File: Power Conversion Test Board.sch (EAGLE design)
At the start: 18 parts, among them U1 LM2678

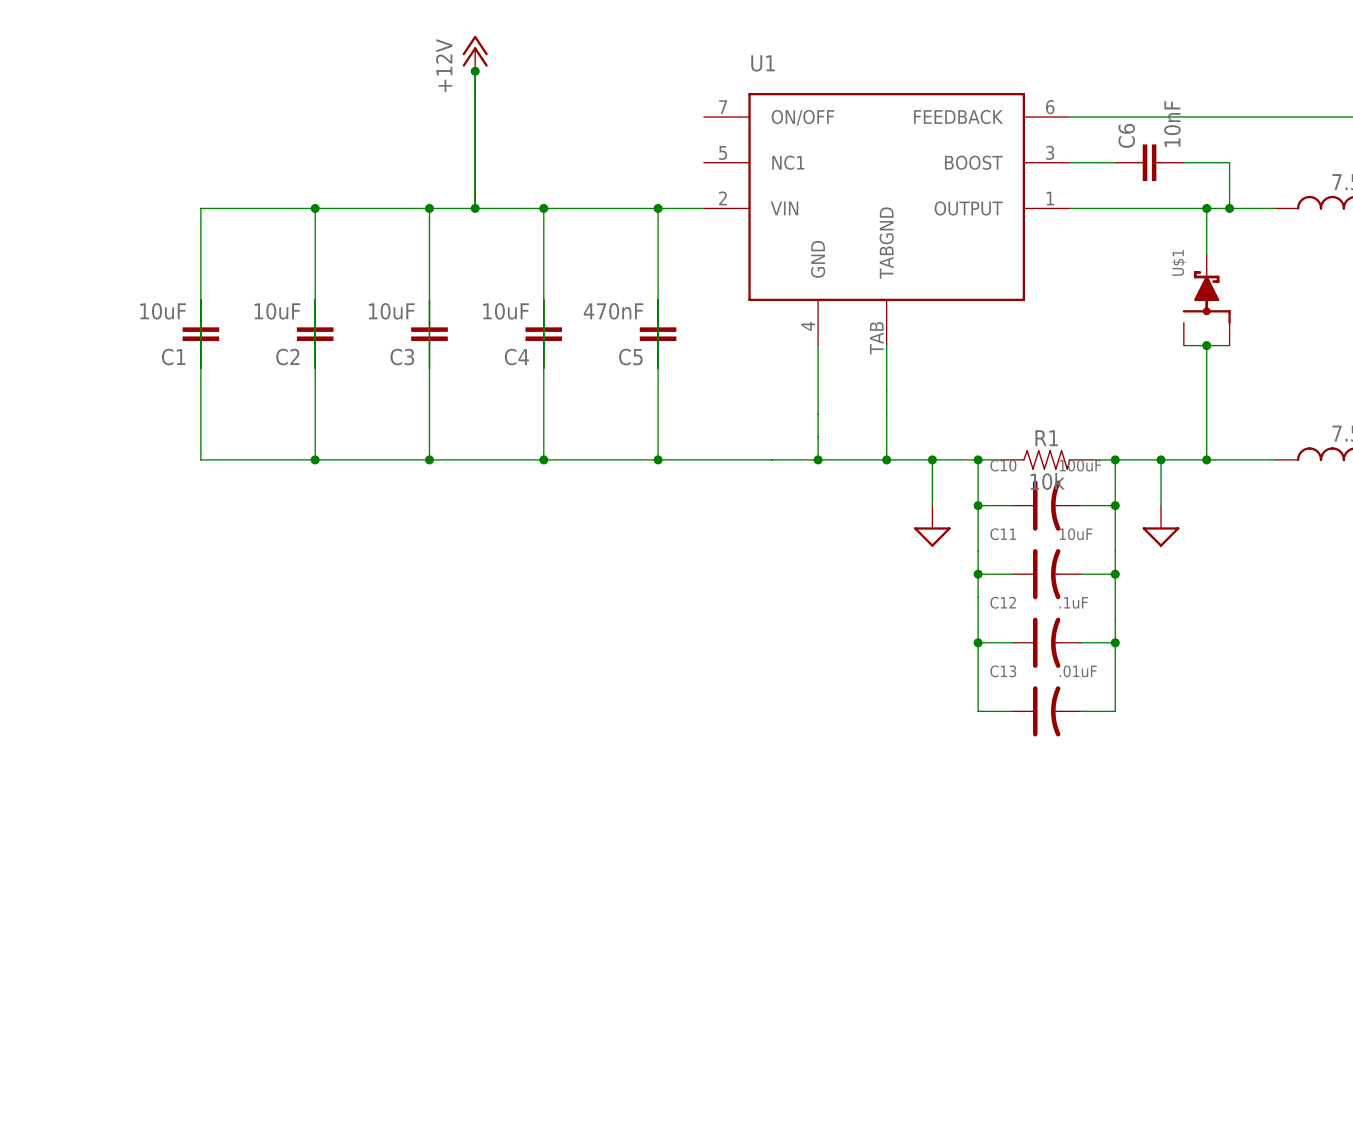
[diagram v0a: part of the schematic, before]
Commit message: Added 3.3V linear regulator
added 3.3V linear regulator and corresponding components
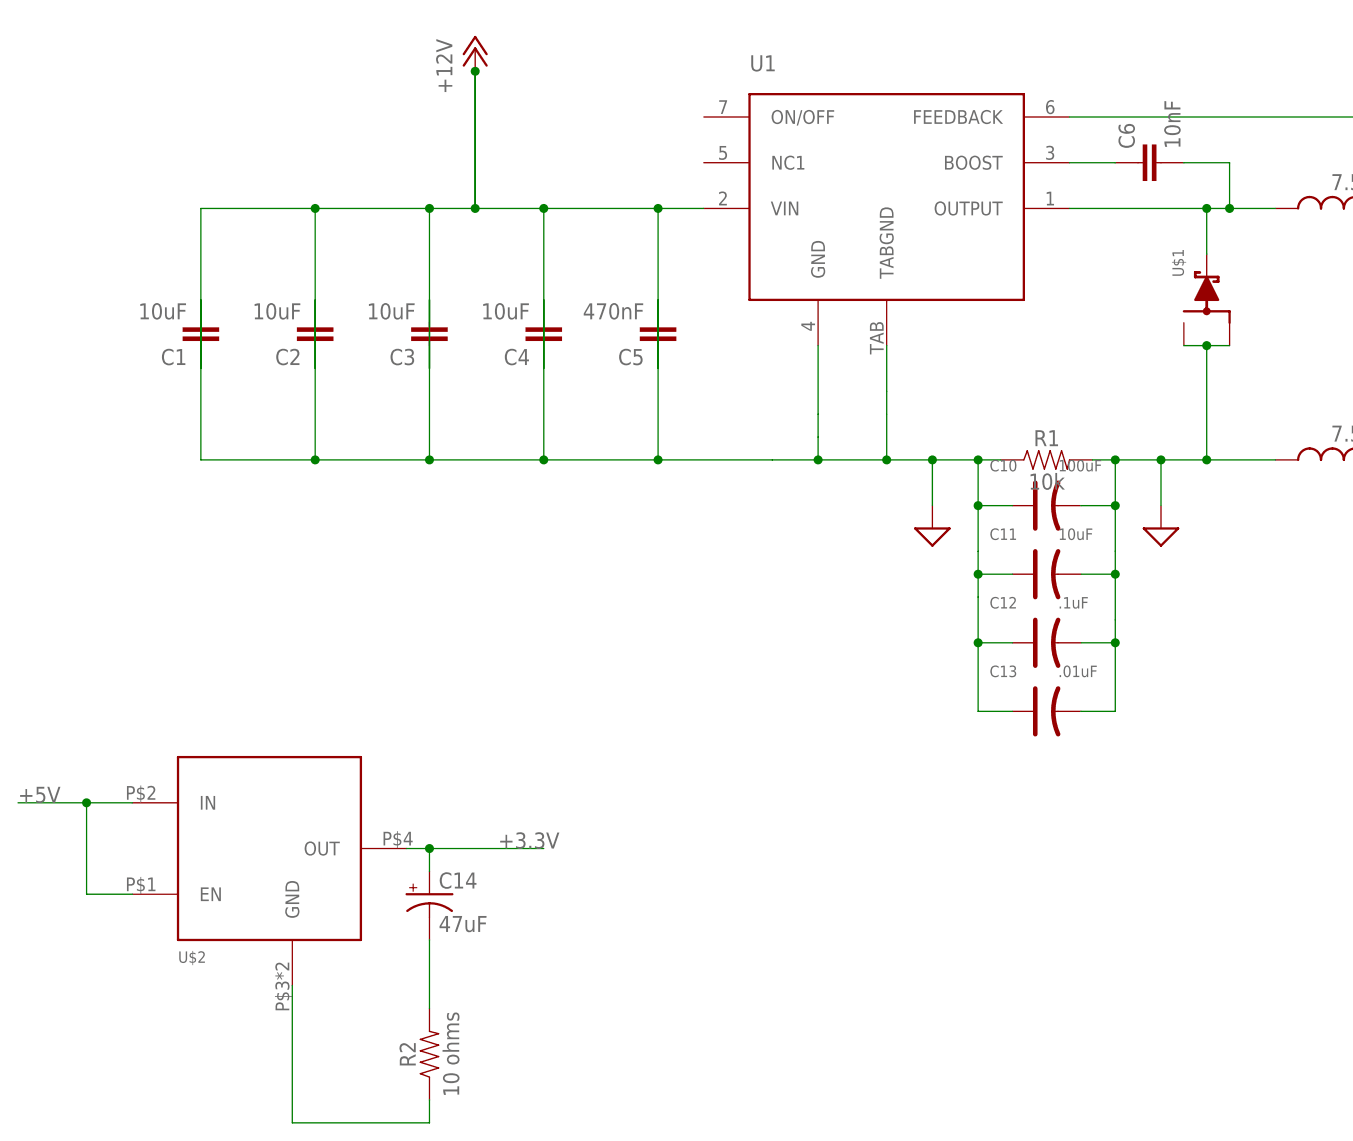
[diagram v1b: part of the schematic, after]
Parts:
- added C14: 47uF, SparkFun-Capacitors:47UF-POLAR-EIA3528-10V-10%
- added R2: 10 ohms, SparkFun-Resistors:RESISTOR0603
- added U$2: TO-263, TPS758:TO-263
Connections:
- new net +3.3V: C14.+, U$2.OUT
- new net N$4: R2.1, U$2.GND
- new net N$5: C14.-, R2.2
- net +5V: now also U$2.EN, U$2.IN
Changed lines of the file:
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@@
 <?xml version="1.0" encoding="utf-8"?>
 <!DOCTYPE eagle SYSTEM "eagle.dtd">
-<eagle version="9.1.3">
+<eagle version="9.2.0">
 <drawing>
 <settings>
@@
 <part name="GND1" library="audio amplifier example" library_urn="urn:adsk.eagle:library:970892" deviceset="GND" device="" value="SUP"/>
 <part name="GND2" library="audio amplifier example" library_urn="urn:adsk.eagle:library:970892" deviceset="GND" device="" value="SUP"/>
+<part name="U$2" library="TPS758" deviceset="TO-263" device=""/>
+<part name="C14" library="SparkFun-Capacitors" library_urn="urn:adsk.eagle:library:510" deviceset="47UF-POLAR" device="-EIA3528-10V-10%" package3d_urn="urn:adsk.eagle:package:37411/1" value="47uF"/>
+<part name="R2" library="SparkFun-Resistors" library_urn="urn:adsk.eagle:library:532" deviceset="RESISTOR" device="0603" package3d_urn="urn:adsk.eagle:package:39650/1" value=" 10 ohms"/>
 </parts>
 <sheets>
@@
 </plain>
 <instances>
-<instance part="FRAME1" gate="G$1" x="0" y="0"/>
-<instance part="C1" gate="G$1" x="76.2" y="129.54" rot="R180"/>
-<instance part="C2" gate="G$1" x="88.9" y="129.54" rot="R180"/>
-<instance part="C3" gate="G$1" x="101.6" y="129.54" rot="R180"/>
-<instance part="C4" gate="G$1" x="114.3" y="129.54" rot="R180"/>
-<instance part="C5" gate="G$1" x="127" y="129.54" rot="R180"/>
-<instance part="C6" gate="G$1" x="182.88" y="147.32" rot="R90"/>
-<instance part="C7" gate="G$1" x="215.9" y="132.08" rot="R270"/>
-<instance part="C8" gate="G$1" x="228.6" y="132.08" rot="R270"/>
-<instance part="C9" gate="G$1" x="241.3" y="132.08" rot="R270"/>
-<instance part="U1" gate="G$1" x="149.86" y="139.7"/>
-<instance part="U$1" gate="G$1" x="187.96" y="134.62" rot="R90"/>
-<instance part="L1" gate="G$1" x="203.2" y="142.24" rot="R90"/>
-<instance part="L2" gate="G$1" x="203.2" y="114.3" rot="R90"/>
-<instance part="P+1" gate="1" x="215.9" y="162.56"/>
-<instance part="P+2" gate="1" x="106.68" y="160.02"/>
-<instance part="R1" gate="G$1" x="170.18" y="114.3"/>
-<instance part="C10" gate="G$1" x="170.18" y="109.22"/>
-<instance part="C11" gate="G$1" x="170.18" y="101.6"/>
-<instance part="C12" gate="G$1" x="170.18" y="93.98"/>
-<instance part="C13" gate="G$1" x="170.18" y="86.36"/>
+<instance part="FRAME1" gate="G$1" x="0" y="0">
+<attribute name="DRAWING_NAME" x="217.17" y="15.24" size="2.54" layer="94"/>
+<attribute name="LAST_DATE_TIME" x="217.17" y="10.16" size="2.286" layer="94"/>
+<attribute name="SHEET" x="230.505" y="5.08" size="2.54" layer="94"/>
+</instance>
+<instance part="C1" gate="G$1" x="76.2" y="129.54" rot="R180">
+<attribute name="NAME" x="74.676" y="126.619" size="1.778" layer="95" font="vector" rot="R180"/>
+<attribute name="VALUE" x="74.676" y="131.699" size="1.778" layer="96" font="vector" rot="R180"/>
+</instance>
+<instance part="C2" gate="G$1" x="88.9" y="129.54" rot="R180">
+<attribute name="NAME" x="87.376" y="126.619" size="1.778" layer="95" font="vector" rot="R180"/>
+<attribute name="VALUE" x="87.376" y="131.699" size="1.778" layer="96" font="vector" rot="R180"/>
+</instance>
+<instance part="C3" gate="G$1" x="101.6" y="129.54" rot="R180">
+<attribute name="NAME" x="100.076" y="126.619" size="1.778" layer="95" font="vector" rot="R180"/>
+<attribute name="VALUE" x="100.076" y="131.699" size="1.778" layer="96" font="vector" rot="R180"/>
+</instance>
+<instance part="C4" gate="G$1" x="114.3" y="129.54" rot="R180">
+<attribute name="NAME" x="112.776" y="126.619" size="1.778" layer="95" font="vector" rot="R180"/>
+<attribute name="VALUE" x="112.776" y="131.699" size="1.778" layer="96" font="vector" rot="R180"/>
+</instance>
+<instance part="C5" gate="G$1" x="127" y="129.54" rot="R180">
+<attribute name="NAME" x="125.476" y="126.619" size="1.778" layer="95" font="vector" rot="R180"/>
+<attribute name="VALUE" x="125.476" y="131.699" size="1.778" layer="96" font="vector" rot="R180"/>
+</instance>
+<instance part="C6" gate="G$1" x="182.88" y="147.32" rot="R90">
+<attribute name="NAME" x="179.959" y="148.844" size="1.778" layer="95" font="vector" rot="R90"/>
+<attribute name="VALUE" x="185.039" y="148.844" size="1.778" layer="96" font="vector" rot="R90"/>
+</instance>
+<instance part="C7" gate="G$1" x="215.9" y="132.08" rot="R270">
+<attribute name="NAME" x="219.71" y="138.43" size="1.27" layer="95" ratio="10" rot="R270"/>
+<attribute name="VALUE" x="219.71" y="130.81" size="1.27" layer="96" ratio="10" rot="R270"/>
+</instance>
+<instance part="C8" gate="G$1" x="228.6" y="132.08" rot="R270">
+<attribute name="NAME" x="232.41" y="138.43" size="1.27" layer="95" ratio="10" rot="R270"/>
+<attribute name="VALUE" x="232.41" y="130.81" size="1.27" layer="96" ratio="10" rot="R270"/>
+</instance>
+<instance part="C9" gate="G$1" x="241.3" y="132.08" rot="R270">
+<attribute name="NAME" x="245.11" y="138.43" size="1.27" layer="95" ratio="10" rot="R270"/>
+<attribute name="VALUE" x="245.11" y="130.81" size="1.27" layer="96" ratio="10" rot="R270"/>
+</instance>
+<instance part="U1" gate="G$1" x="149.86" y="139.7">
+<attribute name="NAME" x="137.16" y="157.48" size="1.778" layer="95"/>
+</instance>
+<instance part="U$1" gate="G$1" x="187.96" y="134.62" rot="R90">
+<attribute name="NAME" x="185.42" y="134.62" size="1.27" layer="95" rot="R90"/>
+</instance>
+<instance part="L1" gate="G$1" x="203.2" y="142.24" rot="R90">
+<attribute name="NAME" x="208.28" y="140.97" size="1.778" layer="95" rot="R180"/>
+<attribute name="VALUE" x="208.28" y="146.05" size="1.778" layer="96" rot="R180"/>
+</instance>
+<instance part="L2" gate="G$1" x="203.2" y="114.3" rot="R90">
+<attribute name="NAME" x="208.28" y="113.03" size="1.778" layer="95" rot="R180"/>
+<attribute name="VALUE" x="208.28" y="118.11" size="1.778" layer="96" rot="R180"/>
+</instance>
+<instance part="P+1" gate="1" x="215.9" y="162.56">
+<attribute name="VALUE" x="213.36" y="157.48" size="1.778" layer="96" rot="R90"/>
+</instance>
+<instance part="P+2" gate="1" x="106.68" y="160.02">
+<attribute name="VALUE" x="104.14" y="154.94" size="1.778" layer="96" rot="R90"/>
+</instance>
+<instance part="R1" gate="G$1" x="170.18" y="114.3">
+<attribute name="NAME" x="170.18" y="115.824" size="1.778" layer="95" font="vector" align="bottom-center"/>
+<attribute name="VALUE" x="170.18" y="112.776" size="1.778" layer="96" font="vector" align="top-center"/>
+</instance>
+<instance part="C10" gate="G$1" x="170.18" y="109.22">
+<attribute name="NAME" x="163.83" y="113.03" size="1.27" layer="95" ratio="10"/>
+<attribute name="VALUE" x="171.45" y="113.03" size="1.27" layer="96" ratio="10"/>
+</instance>
+<instance part="C11" gate="G$1" x="170.18" y="101.6">
+<attribute name="NAME" x="163.83" y="105.41" size="1.27" layer="95" ratio="10"/>
+<attribute name="VALUE" x="171.45" y="105.41" size="1.27" layer="96" ratio="10"/>
+</instance>
+<instance part="C12" gate="G$1" x="170.18" y="93.98">
+<attribute name="NAME" x="163.83" y="97.79" size="1.27" layer="95" ratio="10"/>
+<attribute name="VALUE" x="171.45" y="97.79" size="1.27" layer="96" ratio="10"/>
+</instance>
+<instance part="C13" gate="G$1" x="170.18" y="86.36">
+<attribute name="NAME" x="163.83" y="90.17" size="1.27" layer="95" ratio="10"/>
+<attribute name="VALUE" x="171.45" y="90.17" size="1.27" layer="96" ratio="10"/>
+</instance>
 <instance part="GND1" gate="G$1" x="157.48" y="109.22"/>
 <instance part="GND2" gate="G$1" x="182.88" y="109.22"/>
+<instance part="U$2" gate="G$1" x="83.82" y="71.12">
+<attribute name="NAME" x="73.66" y="58.42" size="1.27" layer="95"/>
+</instance>
+<instance part="C14" gate="G$1" x="101.6" y="66.04">
+<attribute name="NAME" x="102.616" y="66.675" size="1.778" layer="95" font="vector"/>
+<attribute name="VALUE" x="102.616" y="61.849" size="1.778" layer="96" font="vector"/>
+</instance>
+<instance part="R2" gate="G$1" x="101.6" y="48.26" rot="R90">
+<attribute name="NAME" x="100.076" y="48.26" size="1.778" layer="95" font="vector" rot="R90" align="bottom-center"/>
+<attribute name="VALUE" x="103.124" y="48.26" size="1.778" layer="96" font="vector" rot="R90" align="top-center"/>
+</instance>
 </instances>
 <busses>
@@
 <wire x1="172.72" y1="152.4" x2="215.9" y2="152.4" width="0.1524" layer="91"/>
 <junction x="215.9" y="152.4"/>
+</segment>
+<segment>
+<pinref part="U$2" gate="G$1" pin="EN"/>
+<wire x1="68.58" y1="66.04" x2="63.5" y2="66.04" width="0.1524" layer="91"/>
+<wire x1="63.5" y1="66.04" x2="63.5" y2="76.2" width="0.1524" layer="91"/>
+<pinref part="U$2" gate="G$1" pin="IN"/>
+<wire x1="63.5" y1="76.2" x2="68.58" y2="76.2" width="0.1524" layer="91"/>
+<wire x1="63.5" y1="76.2" x2="55.88" y2="76.2" width="0.1524" layer="91"/>
+<junction x="63.5" y="76.2"/>
+<label x="55.88" y="76.2" size="1.778" layer="95"/>
 </segment>
 </net>
@@
 </segment>
 </net>
+<net name="N$4" class="0">
+<segment>
+<pinref part="U$2" gate="G$1" pin="GND"/>
+<wire x1="86.36" y1="55.88" x2="86.36" y2="40.64" width="0.1524" layer="91"/>
+<wire x1="86.36" y1="40.64" x2="101.6" y2="40.64" width="0.1524" layer="91"/>
+<pinref part="R2" gate="G$1" pin="1"/>
+<wire x1="101.6" y1="40.64" x2="101.6" y2="43.18" width="0.1524" layer="91"/>
+</segment>
+</net>
+<net name="N$5" class="0">
+<segment>
+<pinref part="R2" gate="G$1" pin="2"/>
+<pinref part="C14" gate="G$1" pin="-"/>
+<wire x1="101.6" y1="53.34" x2="101.6" y2="60.96" width="0.1524" layer="91"/>
+</segment>
+</net>
+<net name="+3.3V" class="0">
+<segment>
+<pinref part="C14" gate="G$1" pin="+"/>
+<wire x1="101.6" y1="68.58" x2="101.6" y2="71.12" width="0.1524" layer="91"/>
+<pinref part="U$2" gate="G$1" pin="OUT"/>
+<wire x1="101.6" y1="71.12" x2="99.06" y2="71.12" width="0.1524" layer="91"/>
+<wire x1="101.6" y1="71.12" x2="114.3" y2="71.12" width="0.1524" layer="91"/>
+<junction x="101.6" y="71.12"/>
+<label x="109.22" y="71.12" size="1.778" layer="95"/>
+</segment>
+</net>

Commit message: added the right connnections
fixed up the connections on the 3.3V line
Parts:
- removed C14: 47uF, SparkFun-Capacitors:47UF-POLAR-EIA3528-10V-10%
- removed R2: 10 ohms, SparkFun-Resistors:RESISTOR0603
- removed U$2: TO-263, TPS758:TO-263
- added C15, C16, C17, C18: 10uF, SparkFun-Capacitors:10UF-0603-6.3V-20%
- added C19: 470nF, SparkFun-Capacitors:470NF-0402-16V-10%
- added C20: 10nF, SparkFun-Capacitors:10NF-0603-50V-10%
- added C21, C22, C23: 150uf, Seeed-Capacitor:TANTALUM-SMD-10UF-16V-10%(AVX-A)
- added C24: 100uF, Seeed-Capacitor:TANTALUM-SMD-10UF-16V-10%(AVX-A)
- added C25: 10uF, Seeed-Capacitor:TANTALUM-SMD-10UF-16V-10%(AVX-A)
- added C26: .1uF, Seeed-Capacitor:TANTALUM-SMD-10UF-16V-10%(AVX-A)
- added C27: .01uF, Seeed-Capacitor:TANTALUM-SMD-10UF-16V-10%(AVX-A)
- added C28: 47uF, SparkFun-Capacitors:47UF-POLAR-EIA3528-10V-10%
- added L3, L4: 7.5uH, rcl:L-USL2012C
- added R3: 10k, SparkFun-Resistors:10KOHM-0603-1/10W-1%
- added R4: 10 ohms, SparkFun-Resistors:RESISTOR0603
- added U$3: SWITCHMODE_SCHOTTKY, PowerComponents:SWITCHMODE_SCHOTTKY
- added U$4: TO-263, TPS758:TO-263
- added U2: LM2678, PowerComponents:LM2678
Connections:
- removed net N$4: R2.1, U$2.GND
- removed net N$5: C14.-, R2.2
- new net +5V_3.3V: C21.+, C22.+, C23.+, L3.2, U$4.EN, U$4.IN, U2.FEEDBACK
- new net N$10: C28.-, R4.2
- new net N$2: C20.1, U2.BOOST
- new net N$6: C21.-, C22.-, C23.-, L4.2
- new net N$7: C20.2, L3.1, U$3.P$4, U2.OUTPUT
- new net N$9: R4.1, U$4.GND
- net +12V: now also C15.1, C16.1, C17.1, C18.1, C19.1, U2.VIN
- net +3.3V: now also C28.+, U$4.OUT; no longer C14.+, U$2.OUT
- net +5V: no longer U$2.EN, U$2.IN
- net GND: now also C15.2, C16.2, C17.2, C18.2, C19.2, C24.+, C24.-, C25.+, C25.-, C26.+, C26.-, C27.+, C27.-, L4.1, R3.1, R3.2, U$3.P$1, U$3.P$3, U2.GND, U2.TABGND

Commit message: Changed GND signals so they are different for different circuits
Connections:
- new net GND_5V: C10.-, C11.-, C12.-, C13.-, L2.1, R1.2, U$1.P$1, U$1.P$3
- new net GND_5V3: C24.-, C25.-, C26.-, C27.-, L4.1, R3.2, U$3.P$1, U$3.P$3, U2.GND, U2.TABGND
- net GND: no longer C10.-, C11.-, C12.-, C13.-, C24.-, C25.-, C26.-, C27.-, L2.1, L4.1, R1.2, R3.2, U$1.P$1, U$1.P$3, U$3.P$1, U$3.P$3, U2.GND, U2.TABGND
